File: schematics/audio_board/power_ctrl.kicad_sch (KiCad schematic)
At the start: 7 parts, among them Q1 bc847, Q7 dgm2305ux

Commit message: Redesigning audio board to support microphone.
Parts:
- renumbered C15 to C3, Q7 to Q3, R20 to R10, R8 to R15, R9 to R16, R10 to R17
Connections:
- net pwr: now also Q3.2 (S); no longer Q3.3 (D)
- net pwr_out: now also Q3.3 (D); no longer Q3.2 (S)
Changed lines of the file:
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@@
 		(on_board yes)
 		(dnp no)
-		(property "Reference" "#PWR025"
+		(property "Reference" "#PWR012"
 			(at 149.86 110.49 0)
 			(effects
@@
 					(unit 1)
 				)
-				(path "/baedfaab-6940-4c04-b4a7-304f9ffa239d/de9e6a7d-c324-4893-b8ee-7fc82adcf756"
-					(reference "#PWR025")
+				(path "/baedfaab-6940-4c04-b4a7-304f9ffa239d/e0d6a6e0-a9c0-4b3c-93d9-853871b3a3a6"
+					(reference "#PWR012")
 					(unit 1)
 				)
@@
 		(on_board yes)
 		(dnp no)
-		(property "Reference" "R10"
+		(property "Reference" "R17"
 			(at 151.892 82.55 90)
 			(effects
@@
 					(unit 1)
 				)
-				(path "/baedfaab-6940-4c04-b4a7-304f9ffa239d/de9e6a7d-c324-4893-b8ee-7fc82adcf756"
-					(reference "R10")
+				(path "/baedfaab-6940-4c04-b4a7-304f9ffa239d/e0d6a6e0-a9c0-4b3c-93d9-853871b3a3a6"
+					(reference "R17")
 					(unit 1)
 				)
@@
 		(on_board yes)
 		(dnp no)
-		(property "Reference" "R9"
+		(property "Reference" "R16"
 			(at 147.828 68.58 90)
 			(effects
@@
 					(unit 1)
 				)
-				(path "/baedfaab-6940-4c04-b4a7-304f9ffa239d/de9e6a7d-c324-4893-b8ee-7fc82adcf756"
-					(reference "R9")
+				(path "/baedfaab-6940-4c04-b4a7-304f9ffa239d/e0d6a6e0-a9c0-4b3c-93d9-853871b3a3a6"
+					(reference "R16")
 					(unit 1)
 				)
@@
 			(project ""
 				(path "/baedfaab-6940-4c04-b4a7-304f9ffa239d/7706a9b8-079f-4938-b38a-3fd6257c904f"
-					(reference "Q2")
-					(unit 1)
-				)
-				(path "/baedfaab-6940-4c04-b4a7-304f9ffa239d/de9e6a7d-c324-4893-b8ee-7fc82adcf756"
+					(reference "Q1")
+					(unit 1)
+				)
+				(path "/baedfaab-6940-4c04-b4a7-304f9ffa239d/e0d6a6e0-a9c0-4b3c-93d9-853871b3a3a6"
 					(reference "Q1")
 					(unit 1)
@@
 		(on_board yes)
 		(dnp no)
-		(property "Reference" "#PWR026"
+		(property "Reference" "#PWR013"
 			(at 172.72 104.14 0)
 			(effects
@@
 					(unit 1)
 				)
-				(path "/baedfaab-6940-4c04-b4a7-304f9ffa239d/de9e6a7d-c324-4893-b8ee-7fc82adcf756"
-					(reference "#PWR026")
+				(path "/baedfaab-6940-4c04-b4a7-304f9ffa239d/e0d6a6e0-a9c0-4b3c-93d9-853871b3a3a6"
+					(reference "#PWR013")
 					(unit 1)
 				)
@@
 		(on_board yes)
 		(dnp no)
-		(property "Reference" "R8"
+		(property "Reference" "R15"
 			(at 134.62 93.218 90)
 			(effects
@@
 					(unit 1)
 				)
-				(path "/baedfaab-6940-4c04-b4a7-304f9ffa239d/de9e6a7d-c324-4893-b8ee-7fc82adcf756"
-					(reference "R8")
+				(path "/baedfaab-6940-4c04-b4a7-304f9ffa239d/e0d6a6e0-a9c0-4b3c-93d9-853871b3a3a6"
+					(reference "R15")
 					(unit 1)
 				)
@@
 		(on_board yes)
 		(dnp no)
-		(property "Reference" "R20"
+		(property "Reference" "R10"
 			(at 126.238 102.87 90)
 			(effects
@@
 					(unit 1)
 				)
-				(path "/baedfaab-6940-4c04-b4a7-304f9ffa239d/de9e6a7d-c324-4893-b8ee-7fc82adcf756"
-					(reference "R20")
+				(path "/baedfaab-6940-4c04-b4a7-304f9ffa239d/e0d6a6e0-a9c0-4b3c-93d9-853871b3a3a6"
+					(reference "R10")
 					(unit 1)
 				)
@@
 		(on_board yes)
 		(dnp no)
-		(property "Reference" "C15"
+		(property "Reference" "C3"
 			(at 173.355 88.9 0)
 			(effects
@@
 					(unit 1)
 				)
-				(path "/baedfaab-6940-4c04-b4a7-304f9ffa239d/de9e6a7d-c324-4893-b8ee-7fc82adcf756"
-					(reference "C15")
+				(path "/baedfaab-6940-4c04-b4a7-304f9ffa239d/e0d6a6e0-a9c0-4b3c-93d9-853871b3a3a6"
+					(reference "C3")
 					(unit 1)
 				)
@@
 		(on_board yes)
 		(dnp no)
-		(property "Reference" "#PWR022"
+		(property "Reference" "#PWR011"
 			(at 128.27 116.84 0)
 			(effects
@@
 					(unit 1)
 				)
-				(path "/baedfaab-6940-4c04-b4a7-304f9ffa239d/de9e6a7d-c324-4893-b8ee-7fc82adcf756"
-					(reference "#PWR022")
+				(path "/baedfaab-6940-4c04-b4a7-304f9ffa239d/e0d6a6e0-a9c0-4b3c-93d9-853871b3a3a6"
+					(reference "#PWR011")
 					(unit 1)
 				)
@@
 		(lib_id "dgm2305ux:dgm2305ux")
 		(at 158.75 76.2 0)
-		(unit 1)
-		(exclude_from_sim no)
-		(in_bom yes)
-		(on_board yes)
-		(dnp no)
-		(fields_autoplaced yes)
-		(property "Reference" "Q7"
-			(at 165.1 74.9299 0)
+		(mirror x)
+		(unit 1)
+		(exclude_from_sim no)
+		(in_bom yes)
+		(on_board yes)
+		(dnp no)
+		(property "Reference" "Q3"
+			(at 165.1 77.4701 0)
 			(effects
 				(font
@@
 		)
 		(property "Value" "dgm2305ux"
-			(at 165.1 77.4699 0)
+			(at 165.1 74.9301 0)
 			(effects
 				(font
@@
 		)
 		(property "Footprint" "Package_TO_SOT_SMD:SOT-23"
-			(at 163.83 73.66 0)
+			(at 163.83 78.74 0)
 			(effects
 				(font
@@
 		)
 		(property "Datasheet" "https://ngspice.sourceforge.io/docs/ngspice-html-manual/manual.xhtml#cha_MOSFETs"
-			(at 158.75 88.9 0)
+			(at 158.75 63.5 0)
 			(effects
 				(font
@@
 		)
 		(property "Sim.Device" "PMOS"
-			(at 158.75 93.345 0)
+			(at 158.75 59.055 0)
 			(effects
 				(font
@@
 		)
 		(property "Sim.Type" "VDMOS"
-			(at 158.75 95.25 0)
+			(at 158.75 57.15 0)
 			(effects
 				(font
@@
 		)
 		(property "Sim.Pins" "1=D 2=G 3=S"
-			(at 158.75 91.44 0)
+			(at 158.75 60.96 0)
 			(effects
 				(font
@@
 			(project ""
 				(path "/baedfaab-6940-4c04-b4a7-304f9ffa239d/7706a9b8-079f-4938-b38a-3fd6257c904f"
-					(reference "Q8")
-					(unit 1)
-				)
-				(path "/baedfaab-6940-4c04-b4a7-304f9ffa239d/de9e6a7d-c324-4893-b8ee-7fc82adcf756"
 					(reference "Q7")
 					(unit 1)
 				)
+				(path "/baedfaab-6940-4c04-b4a7-304f9ffa239d/e0d6a6e0-a9c0-4b3c-93d9-853871b3a3a6"
+					(reference "Q3")
+					(unit 1)
+				)

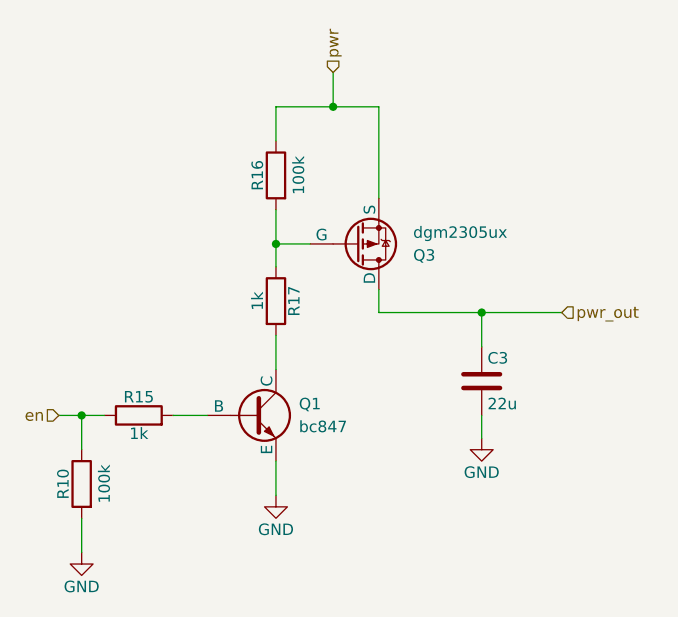
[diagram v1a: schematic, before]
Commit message: Replaced thick film with thin film resistors in feedback loops.
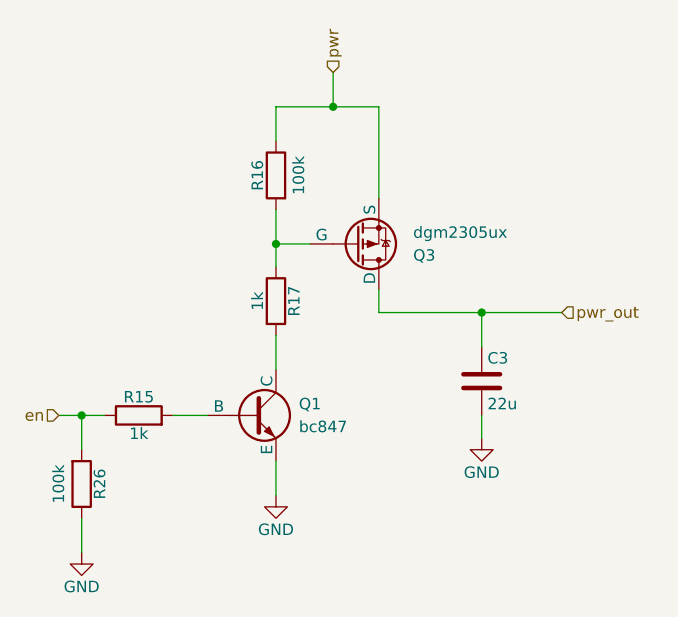
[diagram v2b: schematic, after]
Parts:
- removed R10: 100k, Resistor_SMD:R_0603_1608Metric_Pad0.98x0.95mm_HandSolder, symbol Device:R
- added R26: 100k, Resistor_SMD:R_0603_1608Metric_Pad0.98x0.95mm_HandSolder, symbol Device:R
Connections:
- net GND: now also R26.1
- net en: now also R26.2
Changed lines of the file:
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@@
+	(symbol
+		(lib_id "Device:R")
+		(at 128.27 102.87 0)
+		(mirror x)
+		(unit 1)
+		(exclude_from_sim no)
+		(in_bom yes)
+		(on_board yes)
+		(dnp no)
+		(property "Reference" "R26"
+			(at 130.302 102.87 90)
+			(effects
+				(font
+					(size 1.27 1.27)
+				)
+			)
+		)
+		(property "Value" "100k"
+			(at 125.73 102.87 90)
+			(effects
+				(font
+					(size 1.27 1.27)
+				)
+			)
+		)
+		(property "Footprint" "Resistor_SMD:R_0603_1608Metric_Pad0.98x0.95mm_HandSolder"
+			(at 126.492 102.87 90)
+			(effects
+				(font
+					(size 1.27 1.27)
+				)
+				(hide yes)
+			)
+		)
+		(property "Datasheet" "~"
+			(at 128.27 102.87 0)
+			(effects
+				(font
+					(size 1.27 1.27)
+				)
+				(hide yes)
+			)
+		)
+		(property "Description" "Resistor"
+			(at 128.27 102.87 0)
+			(effects
+				(font
+					(size 1.27 1.27)
+				)
+				(hide yes)
+			)
+		)
+		(property "url" "https://www.digikey.com/en/products/detail/susumu/RG1608P-104-B-T5/1240451"
+			(at 128.27 102.87 90)
+			(effects
+				(font
+					(size 1.27 1.27)
+				)
+				(hide yes)
+			)
+		)
+		(pin "2"
+		)
+		(pin "1"
+		)
+		(instances
+			(project "audio_board"
+				(path "/baedfaab-6940-4c04-b4a7-304f9ffa239d/7706a9b8-079f-4938-b38a-3fd6257c904f"
+					(reference "R33")
+					(unit 1)
+				)
+				(path "/baedfaab-6940-4c04-b4a7-304f9ffa239d/e0d6a6e0-a9c0-4b3c-93d9-853871b3a3a6"
+					(reference "R26")
+					(unit 1)
+				)
+			)
+		)
+	)
 	(symbol
 		(lib_id "Device:R")
@@
 					(unit 1)
 				)
-			)
-		)
-	)
-	(symbol
-		(lib_id "Device:R")
-		(at 128.27 102.87 0)
-		(mirror y)
-		(unit 1)
-		(exclude_from_sim no)
-		(in_bom yes)
-		(on_board yes)
-		(dnp no)
-		(property "Reference" "R10"
-			(at 126.238 102.87 90)
-			(effects
-				(font
-					(size 1.27 1.27)
-				)
-			)
-		)
-		(property "Value" "100k"
-			(at 130.81 102.87 90)
-			(effects
-				(font
-					(size 1.27 1.27)
-				)
-			)
-		)
-		(property "Footprint" "Resistor_SMD:R_0603_1608Metric_Pad0.98x0.95mm_HandSolder"
-			(at 130.048 102.87 90)
-			(effects
-				(font
-					(size 1.27 1.27)
-				)
-				(hide yes)
-			)
-		)
-		(property "Datasheet" "~"
-			(at 128.27 102.87 0)
-			(effects
-				(font
-					(size 1.27 1.27)
-				)
-				(hide yes)
-			)
-		)
-		(property "Description" "Resistor"
-			(at 128.27 102.87 0)
-			(effects
-				(font
-					(size 1.27 1.27)
-				)
-				(hide yes)
-			)
-		)
-		(pin "2"
-		)
-		(pin "1"
-		)
-		(instances
-			(project "audio_board"
-				(path "/baedfaab-6940-4c04-b4a7-304f9ffa239d/7706a9b8-079f-4938-b38a-3fd6257c904f"
-					(reference "R21")
-					(unit 1)
-				)
-				(path "/baedfaab-6940-4c04-b4a7-304f9ffa239d/e0d6a6e0-a9c0-4b3c-93d9-853871b3a3a6"
-					(reference "R10")
-					(unit 1)
-				)
